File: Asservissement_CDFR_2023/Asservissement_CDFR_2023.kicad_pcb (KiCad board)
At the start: 2 copper layers, 86.4 x 114.3 mm, 159 parts, among them IC1 A3930KJPTR-T, IC2 A3930KJPTR-T, J1 Connecteur batterie, J10 Free Connecteur, J11 Conn_01x02, J12 Conn_01x02, J13 Connecteur Odométrie, J2 Conn_01x03, J3 Conn_01x05, J4 Connecteur Programmation, J5 Conn_01x03, J6 Connecteur Odométrie, J7 Conn_01x03, J8 Conn_01x03, J9 Conn_01x05, Q1 QM6006D, Q10 QM6006D, Q11 QM6006D, Q12 QM6006D, Q13 Q_NMOS_GDS, Q2 QM6006D, Q3 QM6006D, Q4 QM6006D, Q5 QM6006D, Q6 QM6006D, Q7 QM6006D, Q8 QM6006D, Q9 QM6006D, U1 LM317_SOT-223, U2 TPS562200, U3 STM32F401RCTx, Y1 Crystal_GND24

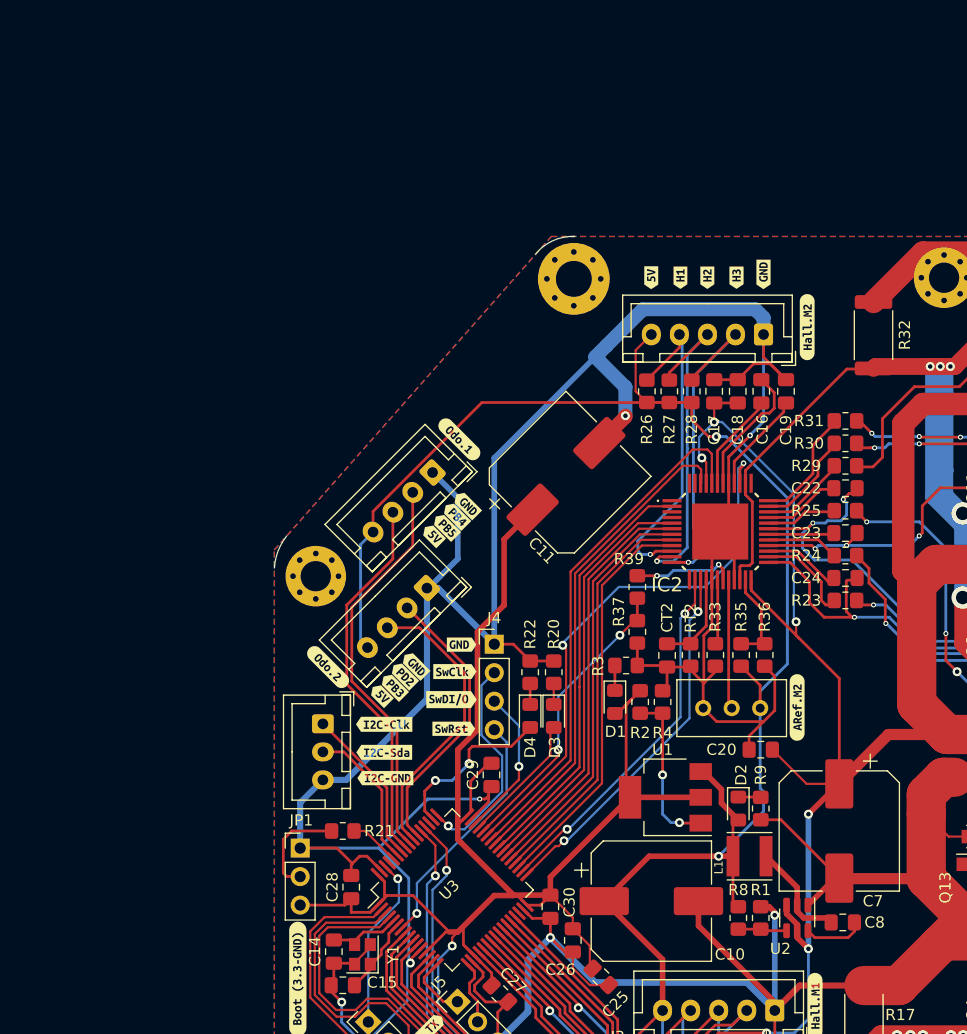
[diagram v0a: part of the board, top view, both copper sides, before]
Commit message: Fix Boost converter
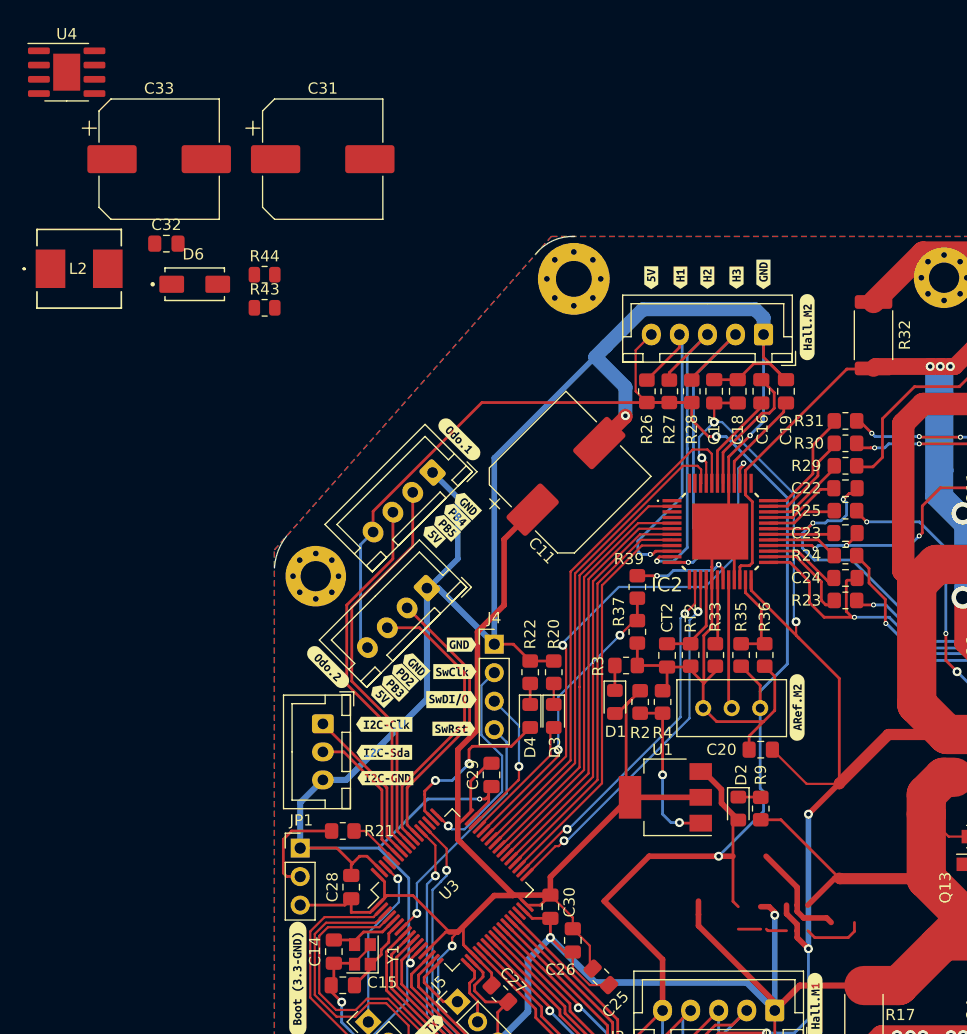
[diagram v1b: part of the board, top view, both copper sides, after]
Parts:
- removed C10, C7: 220u, Capacitor_SMD:CP_Elec_10x10.5
- removed C8: 100nF, Capacitor_SMD:C_0805_2012Metric_Pad1.18x1.45mm_HandSolder
- removed L1: MDA4020-3R3M, Inductor_SMD:L_Vishay_IFSC-1515AH_4x4x1.8mm
- removed R1: 1k, Resistor_SMD:R_0805_2012Metric_Pad1.20x1.40mm_HandSolder
- removed R8: 3.3k, Resistor_SMD:R_0805_2012Metric_Pad1.20x1.40mm_HandSolder
- removed U2: TPS562200, Package_TO_SOT_SMD:SOT-23-6
- added C31: 220uF, Capacitor_SMD:CP_Elec_10x10.5, F.Cu at (39.2, 23.4)
- added C32: 100nF, Capacitor_SMD:C_0805_2012Metric_Pad1.18x1.45mm_HandSolder, F.Cu at (25.3, 30.9)
- added C33: 220uF, Capacitor_SMD:CP_Elec_10x10.5, F.Cu at (24.6, 23.4)
- added D6: DIODE, B170B:DIOM505270X240, F.Cu at (27.8, 34.5)
- added L2: 10uH, IHLP2525CZER100M01:IND_IHLP_2525_CZ-M, F.Cu at (17.5, 33.1)
- added R43: 56k, Resistor_SMD:R_0805_2012Metric, F.Cu at (34.0, 36.6)
- added R44: 10k, Resistor_SMD:R_0805_2012Metric, F.Cu at (34.0, 33.7)
- added U4: LMR16020PDDA, Package_SO:SOIC-8-1EP_3.9x4.9mm_P1.27mm_EP2.41x3.3mm, F.Cu at (16.4, 15.6)
- C11: value 100u -> 100uF
- C27, C28, C29, C30: value 100n -> 100nF
- R11, R12, R13, R26, R27, R28: value R -> 52k
- R37: value 4.7 -> 4.7k
- R39: value 2.2 -> 2.2k
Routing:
- net (no net): track 0.00 -> 18.8 mm
- net Net-(C8-Pad2): track 9.50 -> 0.00 mm
- net Net-(C8-Pad1): track 5.43 -> 0.00 mm
- net Net-(R1-Pad1): track 3.86 -> 0.00 mm

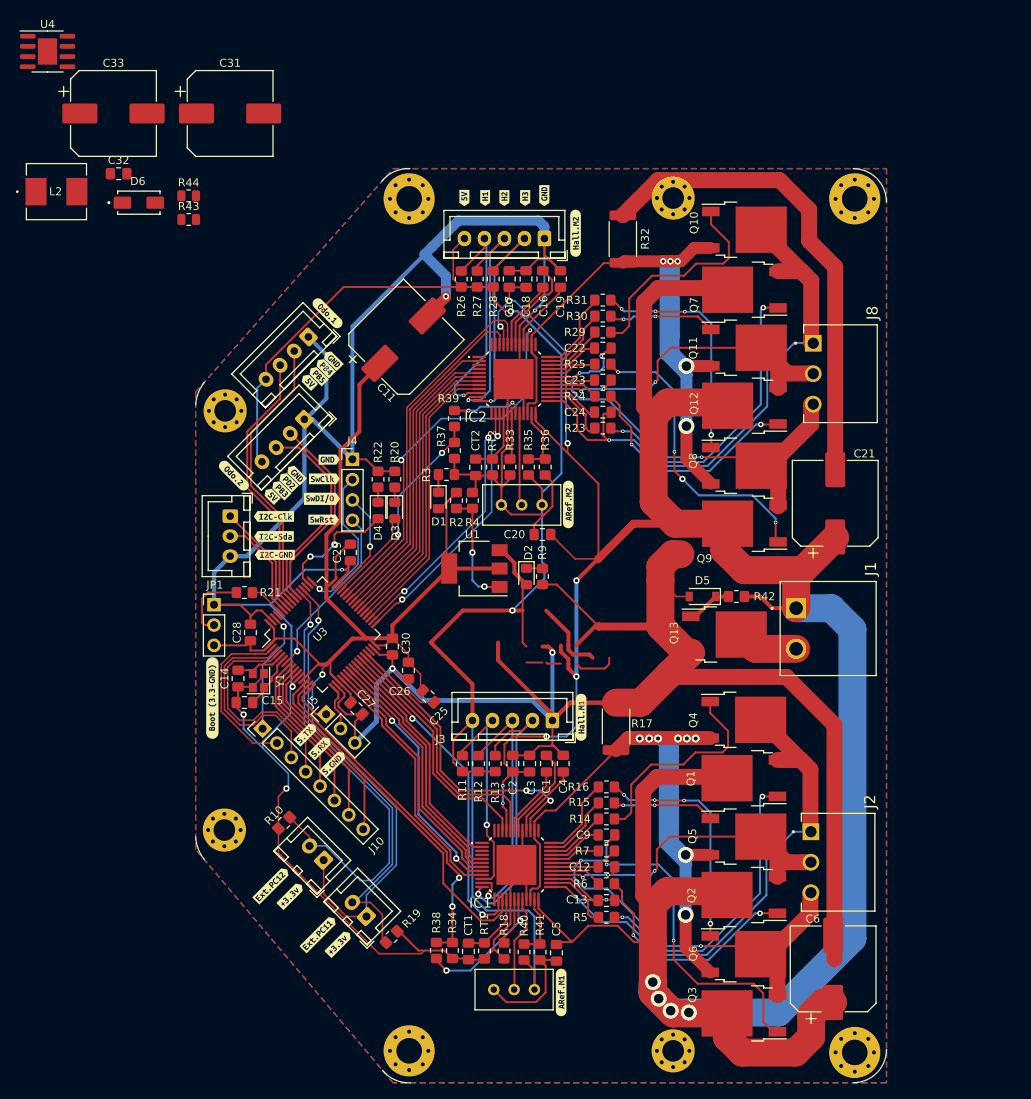
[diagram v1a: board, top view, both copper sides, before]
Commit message: New buck routing + caps removal + fix ground on thermal pad for LMR16020 + removal of curved broder
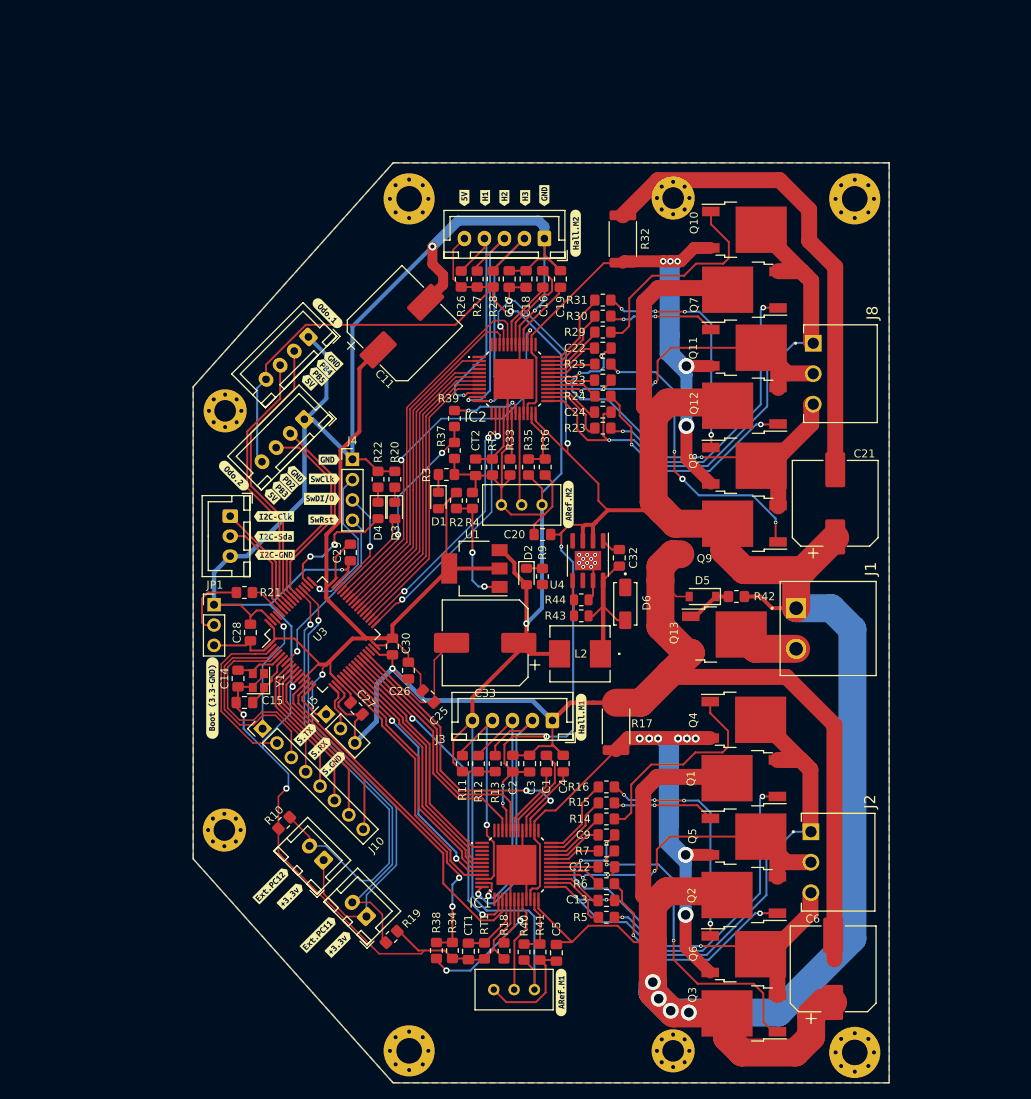
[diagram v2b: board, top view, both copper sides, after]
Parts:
- removed C31: 220uF, Capacitor_SMD:CP_Elec_10x10.5
- moved U4 92.8 mm to (83.9, 79.3), turned to -90 degrees
- moved L2 87.3 mm to (83.0, 90.9), turned to 180 degrees
- moved C33 80.9 mm to (71.1, 89.5), turned to 180 degrees
- moved C32 78.9 mm to (87.9, 78.9), turned to -90 degrees
- moved D6 78.8 mm to (88.6, 84.7), turned to -90 degrees
- moved R44 70.4 mm to (83.1, 84.2)
- moved R43 69.7 mm to (83.1, 86.2), turned to 180 degrees
- moved C11 1.71 mm to (60.7, 50.0)
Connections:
- U4 pad 9: (no net) -> GND
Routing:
- net GND: track 618.4 -> 585.7 mm, vias 8 -> 17
- net (no net): track 18.8 -> 0.00 mm
- net Net-(C32-Pad2): track 0.00 -> 17.9 mm
- net +5V: track 204.8 -> 196.5 mm
- net +BATT: track 390.9 -> 384.7 mm, vias 12 -> 11
- net Net-(R43-Pad2): track 0.00 -> 4.49 mm
- net Net-(C32-Pad1): track 0.00 -> 2.47 mm
- net +3.3V: track 179.4 -> 181.0 mm
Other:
- board size 86.4 x 114.3 mm -> 87 x 115 mm

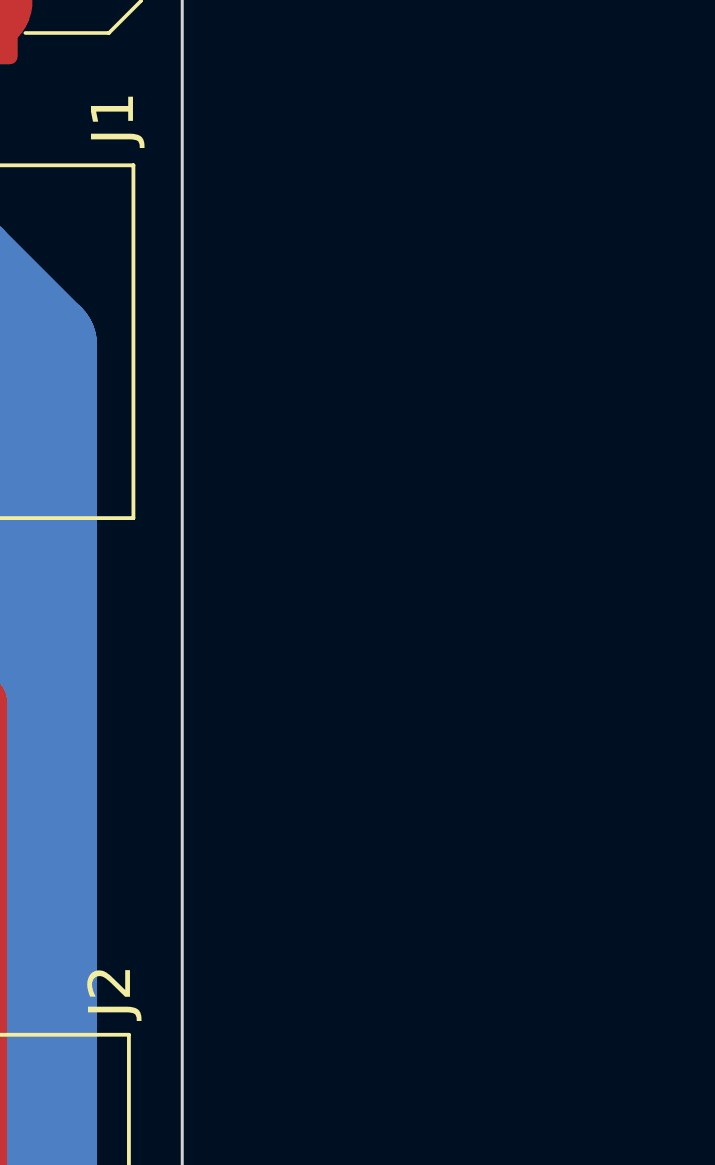
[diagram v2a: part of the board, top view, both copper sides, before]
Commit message: chagement composant
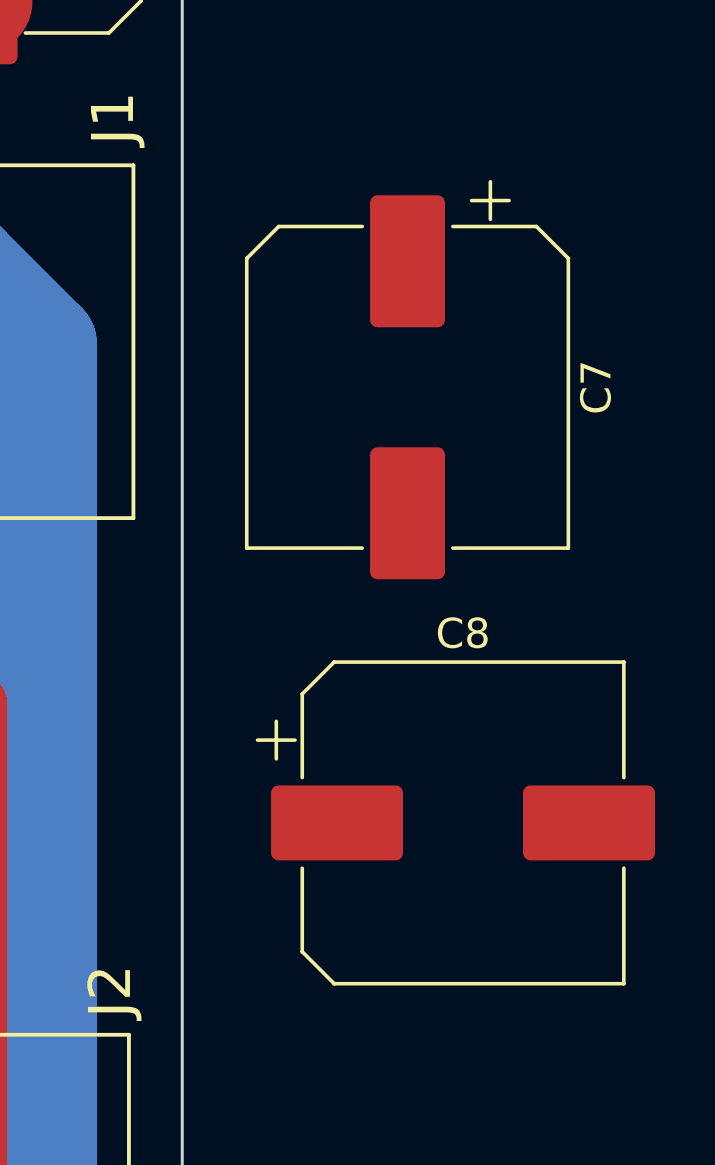
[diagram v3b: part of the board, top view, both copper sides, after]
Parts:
- added C7: 470uF, Capacitor_SMD:CP_Elec_10x10.5, F.Cu at (129.1, 89.3)
- added C8: 470uF, Capacitor_SMD:CP_Elec_10x10.5, F.Cu at (131.0, 103.8)
- C21, C6: value 220uF -> 470uF
- R11, R12, R13, R26, R27, R28: value 52k -> 56k
- R35, R40: value 82k -> 47k
- R36, R41: value 10k -> 15k
- R42: value 50k -> 56k
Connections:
- IC1 pad 3: unconnected-(IC1-Pad3) -> +5V
- IC1 pad 4: unconnected-(IC1-Pad4) -> +5V
- IC2 pad 3: unconnected-(IC2-Pad3) -> +5V
- IC2 pad 4: unconnected-(IC2-Pad4) -> +5V
- R43 pad 1: Net-(C32-Pad2) -> +5V
- U4 pad 4: unconnected-(U4-Pad4) -> GND

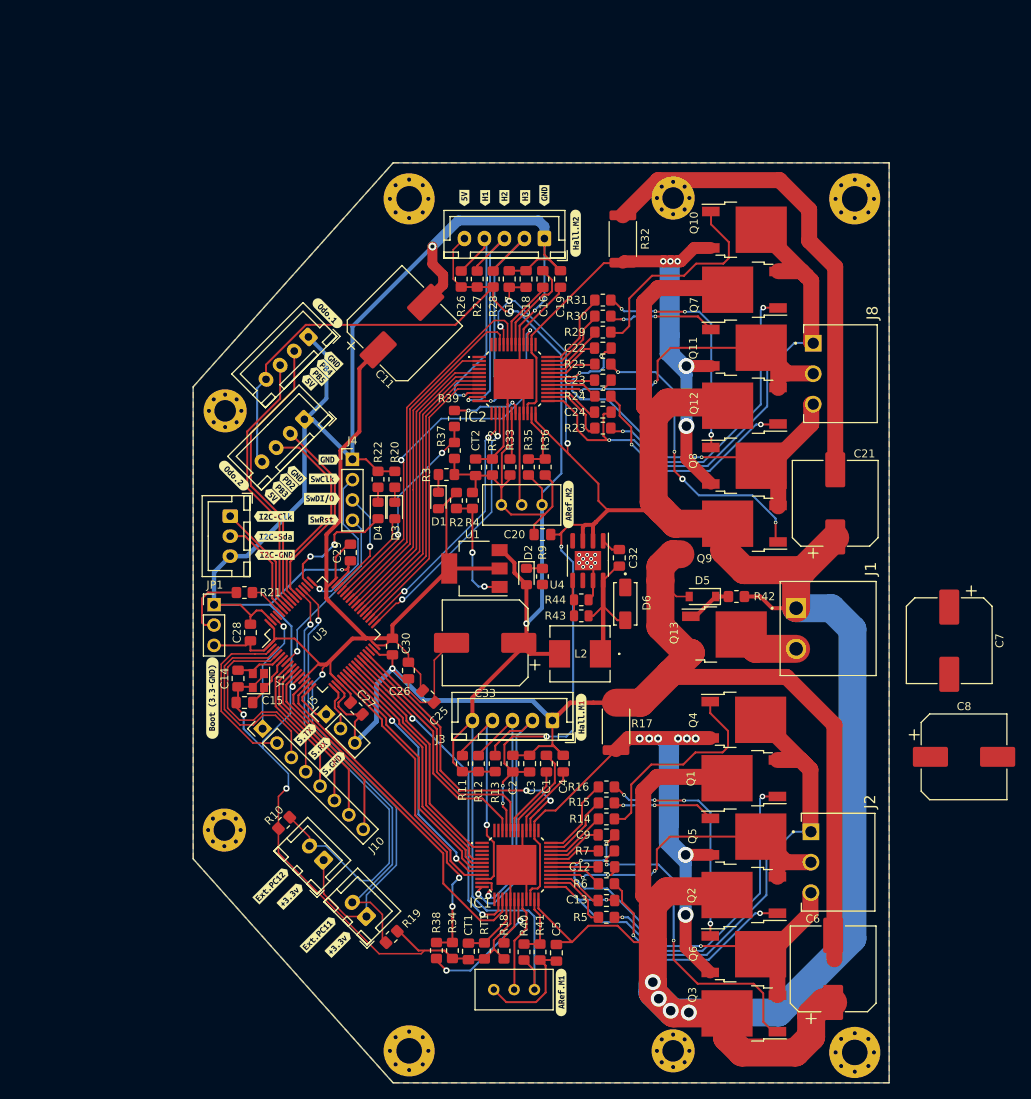
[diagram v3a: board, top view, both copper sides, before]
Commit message: routing updated to match new capacitors
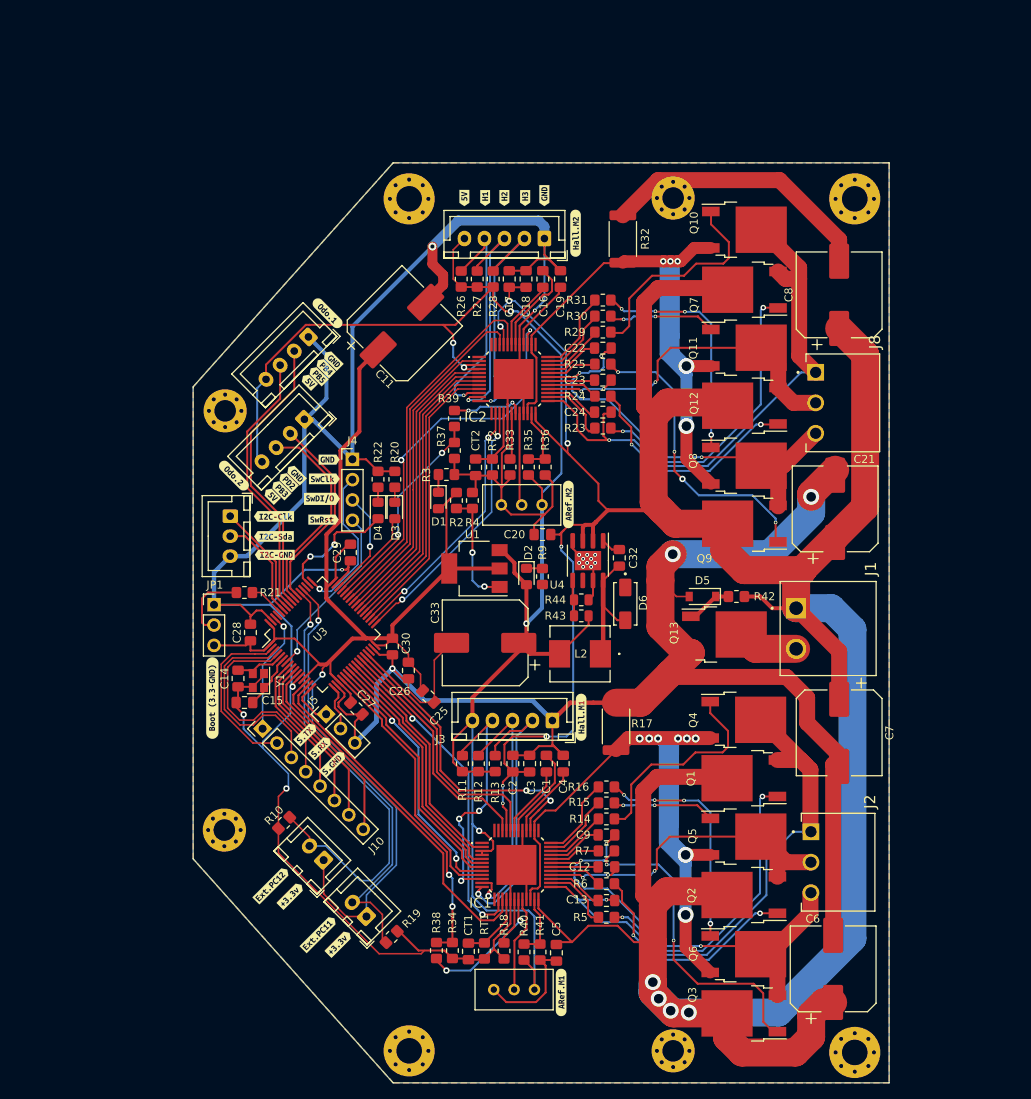
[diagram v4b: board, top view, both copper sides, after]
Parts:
- moved C8 59.8 mm to (115.3, 46.0), turned to 90 degrees
- moved C7 17.9 mm to (115.3, 100.8)
- moved J8 3.65 mm to (112.4, 55.7)
- moved C21 0.69 mm to (114.8, 72.8)
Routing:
- net +BATT: track 384.7 -> 426.4 mm
- net +5V: track 196.5 -> 219.6 mm, vias 2 -> 5
- net Net-(IC1-Pad10): track 27.6 -> 31.6 mm, vias 1 -> 3
- net Net-(C32-Pad2): track 17.9 -> 15.6 mm
- net Net-(C23-Pad2): track 45.4 -> 43.3 mm
- net Net-(C22-Pad2): track 57.6 -> 56.3 mm
- net GND: track 585.7 -> 584.5 mm, vias 17 -> 19
- net Net-(R34-Pad1): track 43.4 -> 42.7 mm
- net frein_1: track 32.6 -> 33.2 mm
